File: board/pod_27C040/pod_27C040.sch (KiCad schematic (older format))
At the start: 13 parts, among them J1 EXT_D, J2 EXT_ADDR, J3 VCC_Probe, J4 GND_Probe, J5 ROM Lines, U1 74HCT02

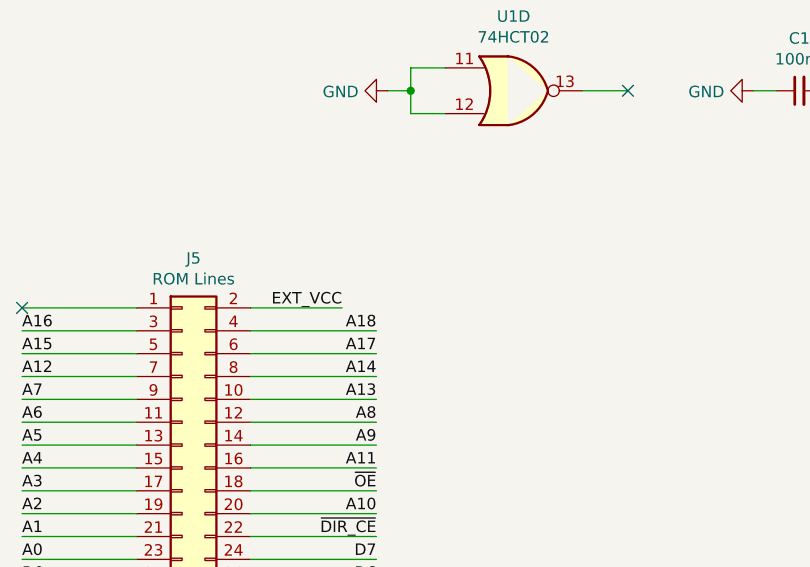
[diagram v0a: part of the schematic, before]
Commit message: Update all the pods to include the diode
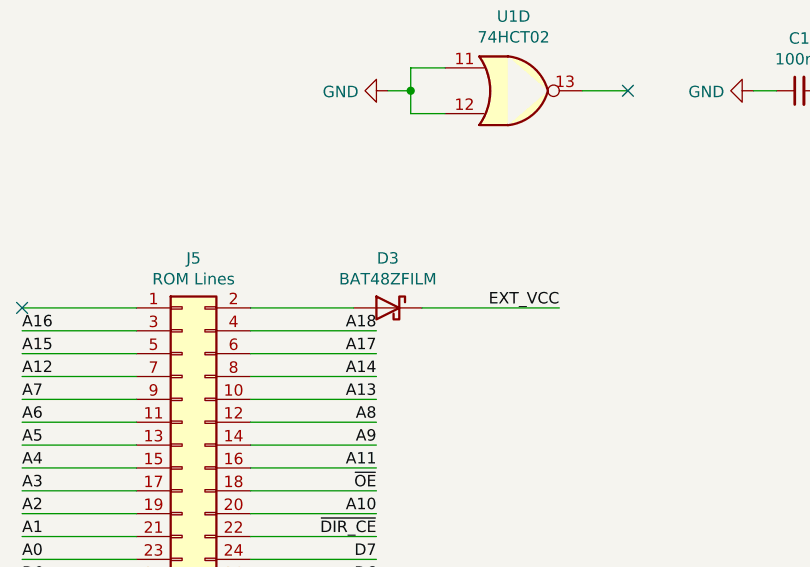
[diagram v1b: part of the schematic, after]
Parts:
- added D3: BAT48ZFILM, Diode_SMD:D_SOD-123, symbol Diode:BAT48ZFILM
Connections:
- net EXT_VCC: now also D3.1 (K); no longer J5.2 (Pin_2)
- new net: D3.2 (A), J5.2 (Pin_2)
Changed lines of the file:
@@
 Wire Wire Line
 	7050 2100 7200 2100
-Wire Wire Line
-	4550 3050 4950 3050
-Text Label 4950 3050 2    50   ~ 0
+Text Label 5900 3050 2    50   ~ 0
 EXT_VCC
 Wire Wire Line
@@
 Text Label 5100 3150 2    50   ~ 0
 A18
+$Comp
+L Diode:BAT48ZFILM D3
+U 1 1 5FD737D6
+P 5150 3050
+F 0 "D3" H 5150 3267 50  0000 C CNN
+F 1 "BAT48ZFILM" H 5150 3176 50  0000 C CNN
+F 2 "Diode_SMD:D_SOD-123" H 5150 2875 50  0001 C CNN
+F 3 "www.st.com/resource/en/datasheet/bat48.pdf" H 5150 3050 50  0001 C CNN
+	1    5150 3050
+	-1   0    0    -1
+$EndComp
+Wire Wire Line
+	5300 3050 5900 3050
+Wire Wire Line
+	5000 3050 4550 3050
 $EndSCHEMATC

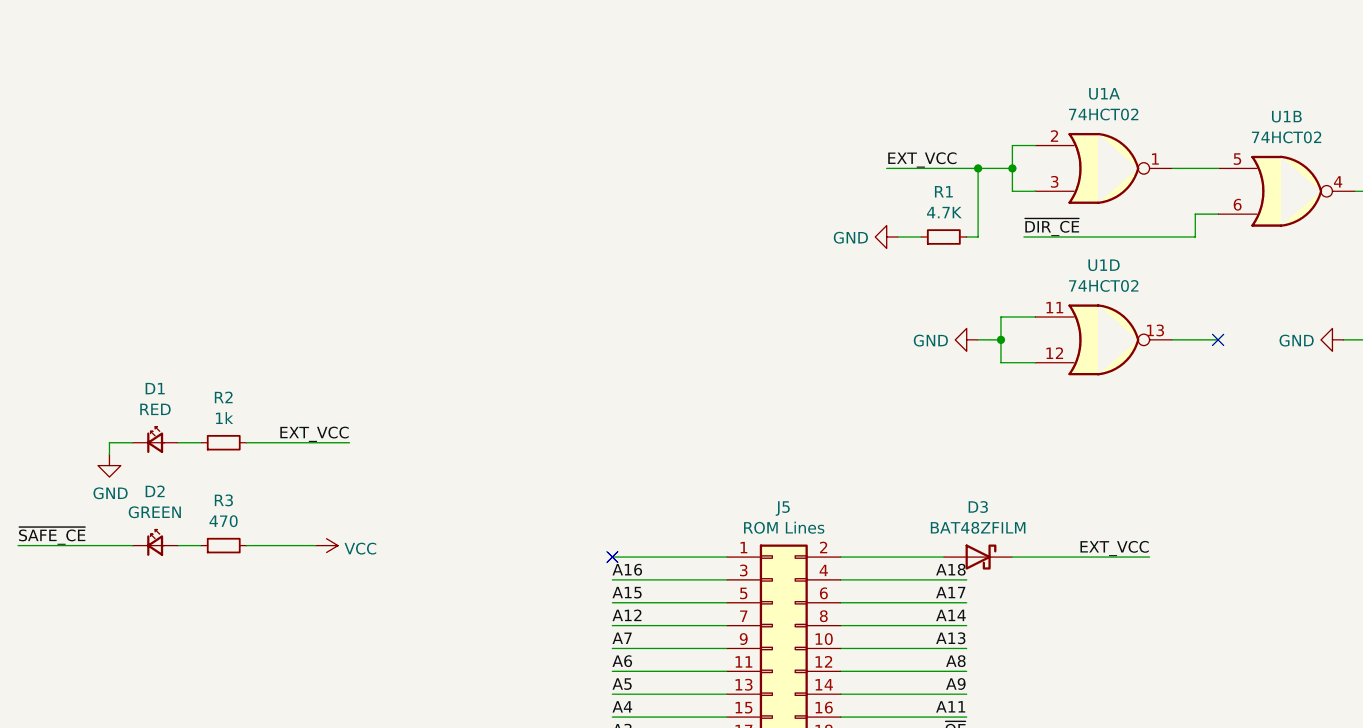
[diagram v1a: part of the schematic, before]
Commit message: Update 27C040 pod
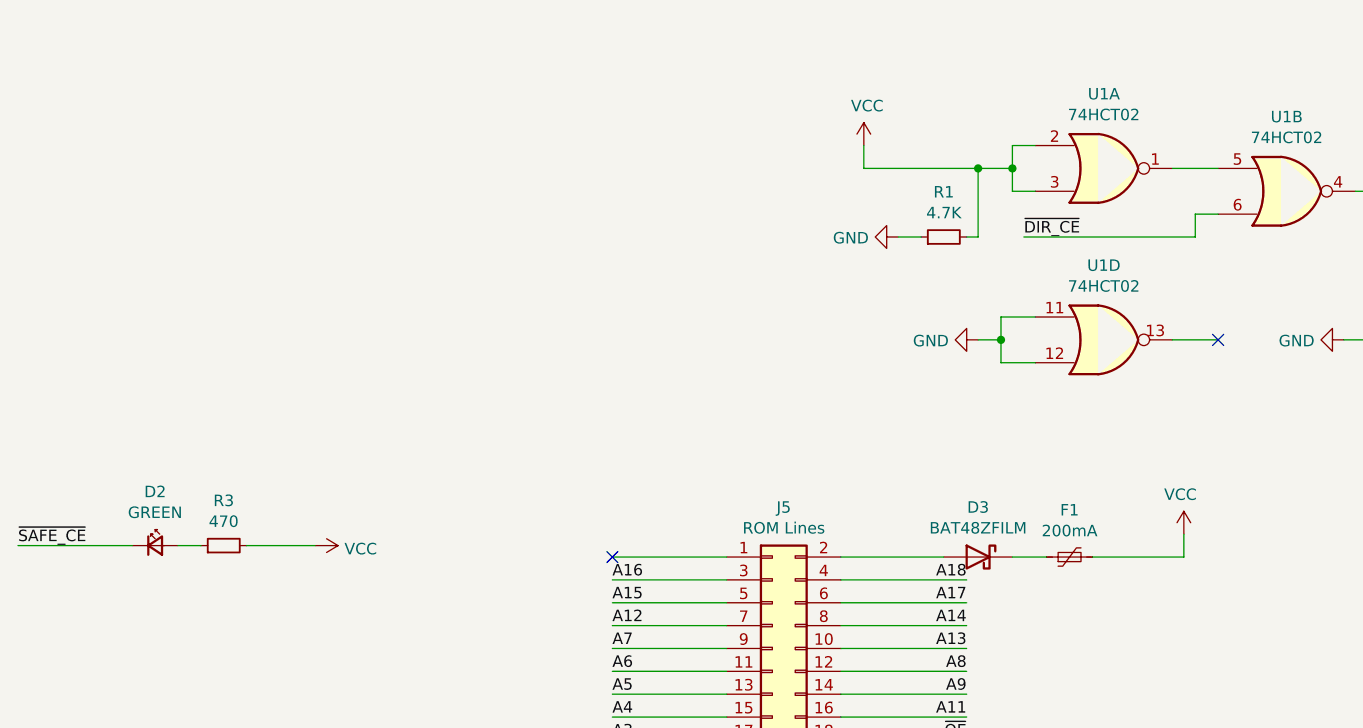
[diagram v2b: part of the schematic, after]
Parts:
- removed D1: RED, LED_SMD:LED_1206_3216Metric, symbol Device:LED_Small
- removed R2: 1k, Resistor_SMD:R_1206_3216Metric, symbol Device:R_Small
- added F1: 200mA, Fuse:Fuse_1206_3216Metric, symbol Device:Polyfuse_Small
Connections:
- net VCC: now also R1.2, U1.2, U1.3, F1.2
- removed net EXT_VCC: D3.1 (K), R1.2, U1.2, U1.3
- new net: D3.1 (K), F1.1
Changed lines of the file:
@@
 Title ""
 Date ""
-Rev ""
+Rev "1.1"
 Comp ""
 Comment1 ""
@@
 Wire Wire Line
 	5300 1350 5300 1450
-Text Label 4750 1350 0    50   ~ 0
-EXT_VCC
 $Comp
 L Device:R_Small R1
@@
 	5150 1650 5150 1350
 Connection ~ 5150 1350
-Wire Wire Line
-	5150 1350 4750 1350
 $Comp
 L power:GND #PWR0109
@@
 Wire Wire Line
 	7050 2100 7200 2100
-Text Label 5900 3050 2    50   ~ 0
-EXT_VCC
 Wire Wire Line
 	4050 4550 3550 4550
@@
 A14
 $Comp
-L Device:LED_Small D1
-U 1 1 601944B8
-P 1550 2550
-F 0 "D1" H 1550 2785 50  0000 C CNN
-F 1 "RED" H 1550 2694 50  0000 C CNN
-F 2 "LED_SMD:LED_1206_3216Metric" V 1550 2550 50  0001 C CNN
-F 3 "~" V 1550 2550 50  0001 C CNN
-	1    1550 2550
-	1    0    0    -1
-$EndComp
-$Comp
-L Device:R_Small R2
-U 1 1 6019F326
-P 1850 2550
-F 0 "R2" V 2046 2550 50  0000 C CNN
-F 1 "1k" V 1955 2550 50  0000 C CNN
-F 2 "Resistor_SMD:R_1206_3216Metric" H 1850 2550 50  0001 C CNN
-F 3 "~" H 1850 2550 50  0001 C CNN
-	1    1850 2550
-	0    -1   -1   0
-$EndComp
-Wire Wire Line
-	1750 2550 1650 2550
-$Comp
-L power:GND #PWR0115
-U 1 1 601B232D
-P 1350 2600
-F 0 "#PWR0115" H 1350 2350 50  0001 C CNN
-F 1 "GND" H 1355 2427 50  0000 C CNN
-F 2 "" H 1350 2600 50  0001 C CNN
-F 3 "" H 1350 2600 50  0001 C CNN
-	1    1350 2600
-	1    0    0    -1
-$EndComp
-Wire Wire Line
-	1450 2550 1350 2550
-Wire Wire Line
-	1350 2550 1350 2600
-Wire Wire Line
-	1950 2550 2400 2550
-Text Label 2400 2550 2    50   ~ 0
-EXT_VCC
-$Comp
 L Device:LED_Small D2
 U 1 1 601DEA89
@@
 $EndComp
 Wire Wire Line
-	5300 3050 5900 3050
-Wire Wire Line
 	5000 3050 4550 3050
+$Comp
+L Device:Polyfuse_Small F1
+U 1 1 600A9122
+P 5550 3050
+F 0 "F1" V 5755 3050 50  0000 C CNN
+F 1 "200mA" V 5664 3050 50  0000 C CNN
+F 2 "Fuse:Fuse_1206_3216Metric" H 5600 2850 50  0001 L CNN
+F 3 "~" H 5550 3050 50  0001 C CNN
+	1    5550 3050
+	0    -1   -1   0
+$EndComp
+$Comp
+L power:VCC #PWR0114
+U 1 1 600E38EB
+P 6050 2950
+F 0 "#PWR0114" H 6050 2800 50  0001 C CNN
+F 1 "VCC" H 6065 3123 50  0000 C CNN
+F 2 "" H 6050 2950 50  0001 C CNN
+F 3 "" H 6050 2950 50  0001 C CNN
+	1    6050 2950
+	-1   0    0    -1
+$EndComp
+Wire Wire Line
+	6050 3050 6050 2950
+Wire Wire Line
+	5300 3050 5450 3050
+Wire Wire Line
+	5650 3050 6050 3050
+$Comp
+L power:VCC #PWR?
+U 1 1 601891C5
+P 4650 1250
+F 0 "#PWR?" H 4650 1100 50  0001 C CNN
+F 1 "VCC" H 4665 1423 50  0000 C CNN
+F 2 "" H 4650 1250 50  0001 C CNN
+F 3 "" H 4650 1250 50  0001 C CNN
+	1    4650 1250
+	1    0    0    -1
+$EndComp
+Wire Wire Line
+	4650 1250 4650 1350
+Wire Wire Line
+	4650 1350 5150 1350
 $EndSCHEMATC
